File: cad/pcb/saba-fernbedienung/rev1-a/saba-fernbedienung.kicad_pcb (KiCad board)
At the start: 4 copper layers, 100 x 81.8 mm, 230 parts, among them J201 Conn_ARM_JTAG_SWD_10, J301 Conn_01x04, J302 Conn_01x04, J303 Micro_SD_Card, J304 Conn_01x04, J305 AudioJack3, J306 Conn_01x02, J307 Conn_01x04, J308 Conn_01x01, J309 Conn_01x01, J310 Conn_01x01, J311 Conn_01x04, J312 Conn_01x08, J313 USB_C_Receptacle_USB2.0, K601 G6K-2, K602 G6K-2, K603 G6K-2, K604 G6K-2, K605 G6K-2, K606 G6K-2, K607 EC2-5TNU, Q201 BC856, Q601 BC846, Q602 BC846, Q603 BC846, Q604 BC846, Q605 BC846, Q606 BC846, Q607 BC846, U201 DOIT-DEVKITV1-ESP32-WROOM-32, U301 TSOP31238, U401 TEC2-0911, U402 1117 1.8V, U403 1117 3.3V, U501 ADA4522-2, U502 LM339, U503 LTV-357T, U504 LTV-357T, U505 LTV-357T, U601 LTV-357T, U701 AD8656, U702 VS1053, Y701 12,288MHz

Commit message: Sicherung
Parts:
- added REF**: OSHW-Logo2_7.3x6mm_SilkScreen, Symbol:OSHW-Logo2_7.3x6mm_SilkScreen, F.Cu at (106.9, 136.8)
- added REF**: OSHW-Logo2_7.3x6mm_Copper, Symbol:OSHW-Logo2_7.3x6mm_Copper, F.Cu at (106.9, 136.8)
- added REF**: MountingHole_3.2mm_M3, MountingHole:MountingHole_3.2mm_M3, F.Cu at (180.0, 101.5)
- added REF**: MountingHole_3.2mm_M3, MountingHole:MountingHole_3.2mm_M3, F.Cu at (170.0, 101.5)
- added REF**: MountingHole_3.2mm_M3, MountingHole:MountingHole_3.2mm_M3, F.Cu at (109.0, 72.5)
- added REF**: MountingHole_3.2mm_M3, MountingHole:MountingHole_3.2mm_M3, F.Cu at (191.0, 72.5)
- added REF**: MountingHole_3.2mm_M3, MountingHole:MountingHole_3.2mm_M3, F.Cu at (191.0, 130.5)
- added REF**: MountingHole_3.2mm_M3, MountingHole:MountingHole_3.2mm_M3, F.Cu at (109.0, 130.5)
- R205, R206, R207, R208: moved to B.Cu
- moved J312 252.9 mm to (111.2, 119.0), turned to 270 degrees
- moved R504 243.7 mm to (84.9, 175.9)
- moved R520 243.7 mm to (101.4, 165.3)
- moved R524 243.7 mm to (96.9, 172.8)
- moved D502 243.7 mm to (80.6, 172.1)
- moved D505 243.7 mm to (81.1, 165.1)
- moved D506 243.7 mm to (89.2, 160.5)
- moved R512 243.7 mm to (88.9, 163.3)
- moved R514 243.7 mm to (88.9, 178.4)
- moved R515 243.7 mm to (96.8, 170.3)
- moved R523 243.7 mm to (88.9, 180.9)
- moved R525 243.7 mm to (100.8, 170.3)
- moved R526 243.7 mm to (92.9, 178.4)
- moved R527 243.7 mm to (96.9, 175.3)
- moved R531 243.7 mm to (76.9, 178.9)
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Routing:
- net SABA_GND_AC: track 16.0 -> 92.8 mm, vias 0 -> 6
- net SABA_Reserve: track 0.00 -> 63.1 mm, vias 0 -> 1
- net SABA_Laut: track 0.00 -> 44.3 mm
- net Net-(J201-Pad6): track 0.00 -> 43.4 mm, vias 0 -> 1
- net SABA_Leise: track 0.00 -> 40.1 mm
- net IR_RX: track 0.00 -> 34.2 mm
- net SABA_15V_AC: track 13.1 -> 46.8 mm, vias 0 -> 2
- net Earth: track 2.30 -> 34.9 mm, vias 1 -> 13
- net LCD_BL: track 0.00 -> 31.2 mm, vias 0 -> 1
- net SABA_Suchlauf_L: track 0.00 -> 29.5 mm
- net SABA_~15V_AC: track 21.8 -> 49.1 mm
- net ~RESET: track 0.00 -> 27.1 mm
- net Net-(J201-Pad4): track 0.00 -> 19.5 mm
- net SABA_Schnelllauf: track 0.00 -> 19.2 mm
- net Net-(J201-Pad8): track 0.00 -> 19.0 mm
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- added copper zone on In2.Cu, net +24V
- added copper zone on B.Cu, net -24V
- added copper zone on In1.Cu, net SABA_GND_AC

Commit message: Sicherung
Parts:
- moved D302 196.4 mm to (144.2, 77.9), turned to 270 degrees
- moved R308 189.9 mm to (137.1, 69.0), turned to 180 degrees
- moved C302 188.8 mm to (128.4, 80.2)
- moved R306 185.2 mm to (140.0, 70.1), turned to 90 degrees
- moved C301 183.6 mm to (128.5, 77.6)
- moved D303 183.0 mm to (140.8, 77.5), turned to 90 degrees
- moved R303 179.7 mm to (149.8, 55.5)
- moved R307 179.7 mm to (141.7, 70.1), turned to 270 degrees
- moved R304 178.2 mm to (135.9, 74.0), turned to 270 degrees
- moved D301 174.5 mm to (149.3, 46.1)
- moved J308 172.7 mm to (152.6, 41.7)
- moved R302 167.3 mm to (149.9, 52.6)
- moved C303 167.0 mm to (144.7, 69.4)
- moved U601 153.7 mm to (139.9, 108.5), turned to 180 degrees
- moved R301 148.9 mm to (149.0, 49.8)
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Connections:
- R205 pad 2: SABA_Suchlauf_L -> SABA_Schnelllauf
- R207 pad 2: SABA_Schnelllauf -> SABA_Suchlauf_L
- U201 pad 17: SABA_Suchlauf_Schnell -> SABA_HS
- U201 pad 19: SABA_HS -> SABA_Suchlauf_Schnell
- U201 pad 26: SABA_Schnelllauf -> SABA_Suchlauf_L
- U201 pad 27: SABA_Suchlauf_L -> SABA_Schnelllauf
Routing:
- net Net-(C503-Pad1): track 0.00 -> 61.3 mm, vias 0 -> 2
- net Net-(R501-Pad1): track 0.00 -> 60.1 mm, vias 0 -> 2
- net SABA_HS: track 0.00 -> 32.3 mm
- net Net-(C402-Pad2): track 0.00 -> 32.0 mm, vias 0 -> 4
- net +24V: track 14.9 -> 44.8 mm, vias 3 -> 7
- net SABA_GND_AC: track 92.8 -> 120.0 mm, vias 6 -> 11
- net Net-(D503-Pad1): track 2.35 -> 29.2 mm
- net SABA_HS3: track 0.00 -> 25.0 mm, vias 0 -> 1
- net Earth: track 34.9 -> 59.7 mm, vias 13 -> 14
- net Net-(D504-Pad1): track 3.26 -> 25.3 mm, vias 0 -> 2
- net /Suchlauf Messung/Phase: track 0.00 -> 18.9 mm, vias 0 -> 2
- net Net-(R515-Pad2): track 0.00 -> 16.8 mm
- net /Suchlauf Messung/Amplitude: track 4.52 -> 20.3 mm, vias 0 -> 2
- net SABA_6,3V_AC: track 0.00 -> 13.7 mm
- net Net-(C402-Pad1): track 0.00 -> 12.8 mm
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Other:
- outline, holes or cut-outs redrawn
- board text added: "Saba 6-3D Serie Automatik Fernbedienung - Webradio"

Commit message: Sicherung
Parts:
- removed R201, R202: 10k, Resistor_SMD:R_0603_1608Metric
- moved C715 175.6 mm to (47.6, 103.4), turned to 270 degrees
- moved R707 170.5 mm to (53.0, 104.8), turned to 270 degrees
- moved C708 167.6 mm to (54.5, 102.9), turned to 90 degrees
- moved C709 165.9 mm to (54.5, 106.7), turned to 90 degrees
- moved C702 163.8 mm to (62.4, 98.3), turned to 270 degrees
- moved C714 163.3 mm to (47.6, 106.4), turned to 90 degrees
- moved R719 158.7 mm to (63.0, 112.0), turned to 90 degrees
- moved C701 158.5 mm to (59.2, 98.3), turned to 270 degrees
- moved R721 158.4 mm to (56.0, 111.8), turned to 90 degrees
- moved C720 156.5 mm to (66.6, 105.6), turned to 270 degrees
- moved R715 152.9 mm to (77.7, 107.7), turned to 90 degrees
- moved C707 152.6 mm to (60.7, 98.6), turned to 270 degrees
- moved R717 151.3 mm to (75.4, 108.4)
- moved C711 149.8 mm to (69.2, 105.5), turned to 180 degrees
- moved R720 148.9 mm to (55.6, 98.9)
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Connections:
- J311 pad 1: SABA_Reserve -> (no net)
- U201 pad 12: Net-(R201-Pad1) -> (no net)
- U201 pad 15: SABA_Laut -> LCD_A0
- U201 pad 4: LCD_A0 -> SABA_Laut
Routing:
- net Earth: track 59.7 -> 147.9 mm, vias 14 -> 69
- net SABA_Reserve: track 66.7 -> 0.00 mm, vias 1 -> 0
- net LCD_A0: track 0.00 -> 41.6 mm
- net +3.3VA: track 0.00 -> 34.9 mm, vias 0 -> 3
- net +5VA: track 0.00 -> 34.4 mm, vias 0 -> 3
- net SABA_Laut: track 44.3 -> 15.8 mm
- net Net-(C705-Pad2): track 0.00 -> 26.8 mm
- net +3V3: track 5.72 -> 30.7 mm, vias 0 -> 6
- net LCD_BL: track 31.2 -> 6.49 mm, vias 1 -> 0
- net Net-(J313-PadS1): track 0.00 -> 20.7 mm
- net Net-(C303-Pad1): track 0.00 -> 20.2 mm
- net Net-(D301-Pad1): track 0.00 -> 19.0 mm
- net +1V8: track 0.00 -> 18.5 mm, vias 0 -> 2
- net Net-(R705-Pad2): track 0.00 -> 18.0 mm
- net Net-(C716-Pad2): track 0.00 -> 16.9 mm
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- added copper zone on F.Cu, net +5V
- added copper zone on F.Cu, net Earth
- added copper zone on In1.Cu, net Earth
- added copper zone on F.Cu, net Net-(C401-Pad1)
- added copper zone on F.Cu, net Net-(C402-Pad1)
- added copper zone on F.Cu, net Net-(C402-Pad2)
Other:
- outline, holes or cut-outs redrawn

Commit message: Sicherung
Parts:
- moved R719 63.9 mm to (126.6, 105.6), turned to 180 degrees
- moved C414 63.5 mm to (123.6, 107.5)
- moved C717 59.7 mm to (135.1, 94.7)
- moved C721 59.7 mm to (131.9, 102.3)
- moved C722 59.7 mm to (131.9, 103.8)
- moved R716 59.7 mm to (134.9, 102.3)
- moved R717 59.7 mm to (134.9, 103.8)
- moved R718 59.7 mm to (134.9, 98.3)
- moved C703 59.7 mm to (114.0, 105.1)
- moved C704 59.7 mm to (120.4, 107.4)
- moved C707 59.7 mm to (120.2, 94.0)
- moved C708 59.7 mm to (114.0, 98.3)
- moved C709 59.7 mm to (114.0, 102.1)
- moved R707 59.7 mm to (112.5, 100.2)
- moved C417 59.7 mm to (129.6, 97.7)
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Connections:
- J312 pad 4: LCD_A0 -> ~RESET
- J312 pad 8: ~RESET -> LCD_A0
- R206 pad 2: SPI_CS_LCD -> SABA_Leise
- U201 pad 23: SABA_Leise -> SPI_CS_LCD
- U201 pad 3: SPI_CS_LCD -> SABA_Leise
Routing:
- net SPI_MOSI: track 2.86 -> 67.3 mm, vias 1 -> 3
- net SABA_Mute: track 0.00 -> 45.0 mm, vias 0 -> 2
- net Net-(R203-Pad2): track 0.00 -> 38.5 mm, vias 0 -> 1
- net SPI_SCK: track 2.84 -> 39.9 mm
- net ~RESET: track 29.3 -> 65.4 mm
- net SPI_CS_SDCARD: track 0.00 -> 30.8 mm, vias 0 -> 1
- net SPI_CS_VS1053: track 0.00 -> 26.4 mm, vias 0 -> 1
- net SPI_MISO: track 2.24 -> 25.8 mm
- net VS1053_DREQ: track 2.62 -> 14.4 mm
- net SPI_CS_LCD: track 2.10 -> 10.2 mm
- net LCD_A0: track 41.6 -> 34.2 mm
- net Net-(C715-Pad1): track 9.02 -> 12.5 mm
- net LCD_BL: track 6.49 -> 9.88 mm, vias 0 -> 1
- net +1V8: track 18.5 -> 21.8 mm, vias 2 -> 3
- net Net-(C714-Pad1): track 9.21 -> 11.8 mm
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
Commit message: PCB: Alle Leitungen verlegt
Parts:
- C407: footprint Capacitor_THT:CP_Radial_D10.0mm_P5.00mm -> local:CP_Radial_D10.0mm_P5.00mm_liegend
- moved R715 12.3 mm to (127.4, 95.6)
- moved C719 12.0 mm to (127.4, 92.5)
- moved C717 9.91 mm to (125.4, 92.5), turned to 270 degrees
- moved R711 6.70 mm to (125.4, 95.6)
- moved R402 1.95 mm to (109.4, 91.5)
- moved C417 0.43 mm to (129.6, 97.3)
- moved R702 0.36 mm to (116.8, 81.8)
- moved C710 0.17 mm to (116.8, 86.6)
- moved R703 0.17 mm to (116.8, 83.6)
- moved R704 0.17 mm to (116.8, 85.1)
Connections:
- C301 pad 2: Earth -> GND
- C302 pad 2: Earth -> GND
- C303 pad 2: Earth -> GND
- C304 pad 2: Earth -> GND
- C406 pad 2: Earth -> GND
- C407 pad 2: Earth -> GND
- C409 pad 1: Earth -> GND
- C412 pad 2: Earth -> GND
- C413 pad 2: Earth -> GND
- C414 pad 2: Earth -> GND
- C415 pad 2: Earth -> GND
- C416 pad 2: Earth -> GND
- C417 pad 2: Earth -> GND
- C506 pad 1: Earth -> GND
- C507 pad 1: Earth -> GND
- C508 pad 1: Earth -> GND
- C601 pad 1: Earth -> GND
- C701 pad 1: Earth -> GND
- C702 pad 1: Earth -> GND
- C703 pad 1: Earth -> GND
- C704 pad 1: Earth -> GND
- C706 pad 1: Earth -> GND
- C707 pad 1: Earth -> GND
- C708 pad 1: Earth -> GND
- C709 pad 1: Earth -> GND
- C710 pad 1: Earth -> GND
- C711 pad 1: Earth -> GND
- C712 pad 1: Earth -> GND
- C713 pad 1: Earth -> GND
- C714 pad 2: Earth -> GND
- C715 pad 2: Earth -> GND
- C718 pad 2: Earth -> GND
- C720 pad 2: Earth -> GND
- C721 pad 2: Earth -> GND
- C722 pad 2: Earth -> GND
- C723 pad 2: Earth -> GND
- C724 pad 2: Earth -> GND
- C725 pad 2: Earth -> GND
- D201 pad 1: Earth -> GND
- D301 pad 3: Earth -> GND
- D303 pad 2: Earth -> GND
- J201 pad 3: Earth -> GND
- J201 pad 5: Earth -> GND
- J201 pad 9: Earth -> GND
- J303 pad 6: Earth -> GND
- J305 pad T: Earth -> GND
- J308 pad 1: Earth -> GND
- J312 pad 7: Earth -> GND
- J313 pad A1: Earth -> GND
- J313 pad A12: Earth -> GND
- J313 pad B1: Earth -> GND
- J313 pad B12: Earth -> GND
- Q601 pad 2: Earth -> GND
- Q602 pad 2: Earth -> GND
- Q603 pad 2: Earth -> GND
- Q604 pad 2: Earth -> GND
- Q605 pad 2: Earth -> GND
- Q606 pad 2: Earth -> GND
- Q607 pad 2: Earth -> GND
- R304 pad 1: Earth -> GND
- R306 pad 1: Earth -> GND
- R307 pad 2: Earth -> GND
- R308 pad 1: Earth -> GND
- R401 pad 1: Earth -> GND
- R402 pad 1: Earth -> GND
- R604 pad 1: Earth -> GND
- R605 pad 1: Earth -> GND
- R610 pad 1: Earth -> GND
- R611 pad 1: Earth -> GND
- R615 pad 1: Earth -> GND
- R616 pad 1: Earth -> GND
- R623 pad 1: Earth -> GND
- R704 pad 2: Earth -> GND
- R705 pad 1: Earth -> GND
- R706 pad 1: Earth -> GND
- R712 pad 2: Earth -> GND
- R713 pad 1: Earth -> GND
- R714 pad 1: Earth -> GND
- R719 pad 1: Earth -> GND
- R720 pad 1: Earth -> GND
- R721 pad 1: Earth -> GND
- U201 pad 2: Earth -> GND
- U201 pad 29: Earth -> GND
- U301 pad 1: Earth -> GND
- U401 pad 7: Earth -> GND
- U402 pad 1: Earth -> GND
- U403 pad 1: Earth -> GND
- U503 pad 3: Earth -> GND
- U504 pad 3: Earth -> GND
- U505 pad 3: Earth -> GND
- U601 pad 3: Earth -> GND
- U701 pad 4: Earth -> GND
- U702 pad 16: Earth -> GND
- U702 pad 20: Earth -> GND
- U702 pad 21: Earth -> GND
- U702 pad 22: Earth -> GND
- U702 pad 35: Earth -> GND
- U702 pad 37: Earth -> GND
- U702 pad 4: Earth -> GND
- U702 pad 40: Earth -> GND
- U702 pad 41: Earth -> GND
- U702 pad 47: Earth -> GND
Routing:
- net GND: track 0.00 -> 171.5 mm, vias 0 -> 76
- net Earth: track 150.4 -> 17.9 mm, vias 69 -> 0
- net +5V: track 24.7 -> 131.5 mm, vias 2 -> 13
- net SPI_SCK: track 39.9 -> 68.2 mm, vias 1 -> 3
- net SPI_MISO: track 25.8 -> 53.9 mm, vias 1 -> 2
- net SABA_Leise: track 39.8 -> 16.0 mm
- net SPI_DCS_VS1053: track 0.00 -> 21.3 mm, vias 0 -> 2
- net +3V3: track 30.7 -> 48.9 mm, vias 6 -> 12
- net Net-(R715-Pad1): track 12.8 -> 28.6 mm
- net +1V8: track 21.8 -> 35.1 mm, vias 3 -> 6
- net /Audio/links: track 2.26 -> 11.4 mm
- net Net-(R713-Pad2): track 8.14 -> 14.0 mm
- net /Audio/rechts: track 7.87 -> 13.7 mm
- net Net-(R619-Pad2): track 0.00 -> 4.89 mm
- net SABA_Mute: track 45.0 -> 40.7 mm, vias 2 -> 1
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- added copper zone on In2.Cu, net +1V8
- added copper zone on In2.Cu, net +3.3VA
- added copper zone on In2.Cu, net +3V3
- added copper zone on In2.Cu, net +5V
- added copper zone on F.Cu, net GND
- added copper zone on In1.Cu, net GND
- removed copper zone on F.Cu, net Earth
- removed copper zone on In1.Cu, net Earth

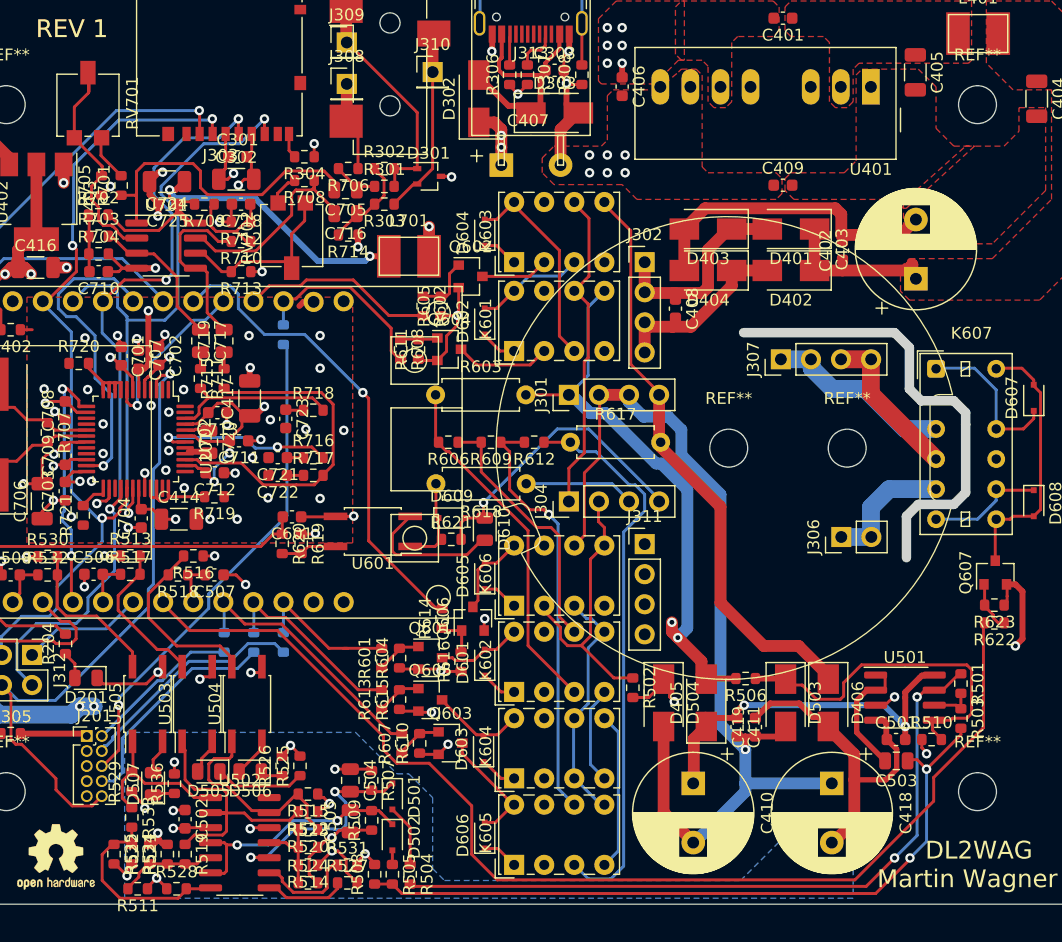
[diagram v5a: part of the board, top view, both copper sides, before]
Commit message: Fix: DRC Fehler
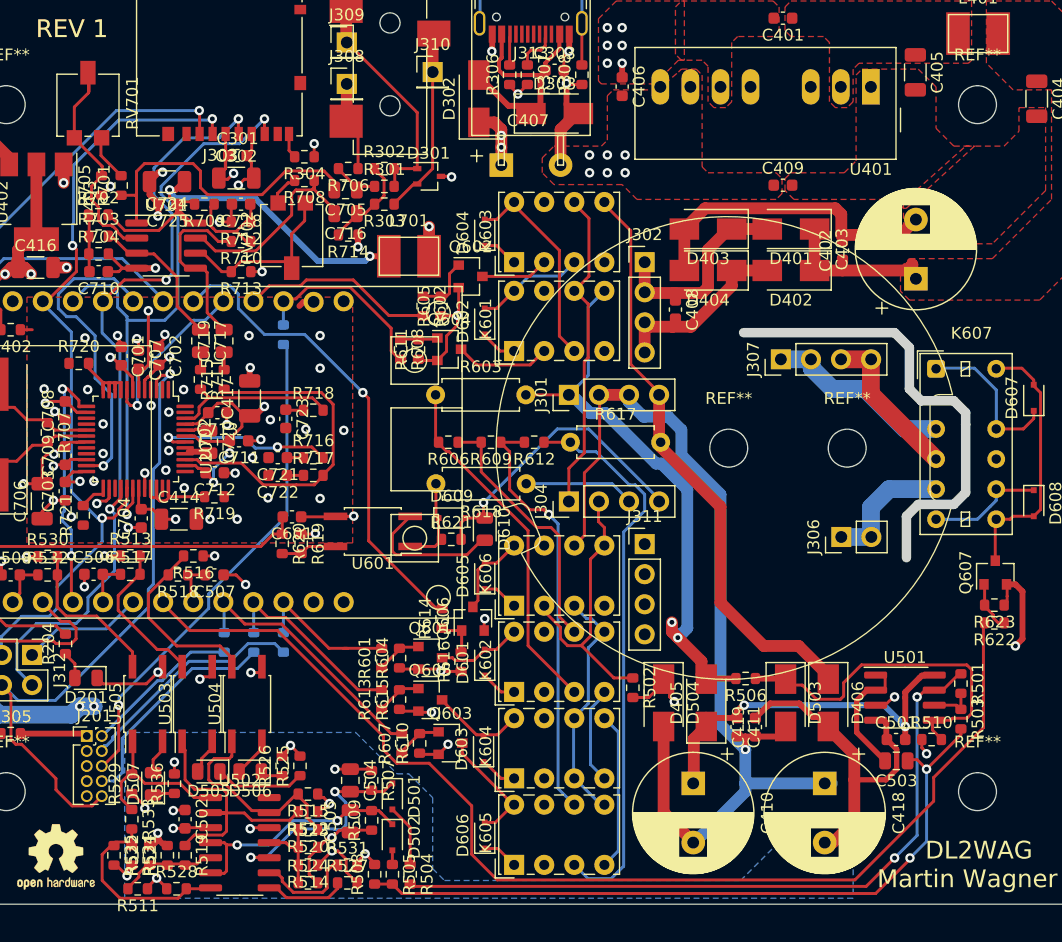
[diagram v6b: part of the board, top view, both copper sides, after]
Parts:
- moved C418 0.60 mm to (178.1, 129.8)
- moved R529 0.15 mm to (119.6, 129.8)
- moved R533 0.15 mm to (119.6, 132.8)
- moved C301 0.10 mm to (128.5, 76.8)
- moved C302 0.10 mm to (128.4, 78.7)
- moved R519 0.10 mm to (124.1, 135.9)
- moved R521 0.10 mm to (122.6, 135.9)
- moved R522 0.10 mm to (121.1, 135.9)
- moved R534 0.10 mm to (119.6, 135.9)
- moved R535 0.10 mm to (118.1, 135.9)
- moved C408 0.08 mm to (165.5, 89.8)
- moved R711 0.08 mm to (125.4, 95.7)
- moved R715 0.08 mm to (127.4, 95.7)
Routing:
- net Net-(R719-Pad2): track 4.87 -> 5.79 mm
- net SABA_GND_AC: track 120.0 -> 120.8 mm
- net Net-(C402-Pad2): track 26.1 -> 26.7 mm

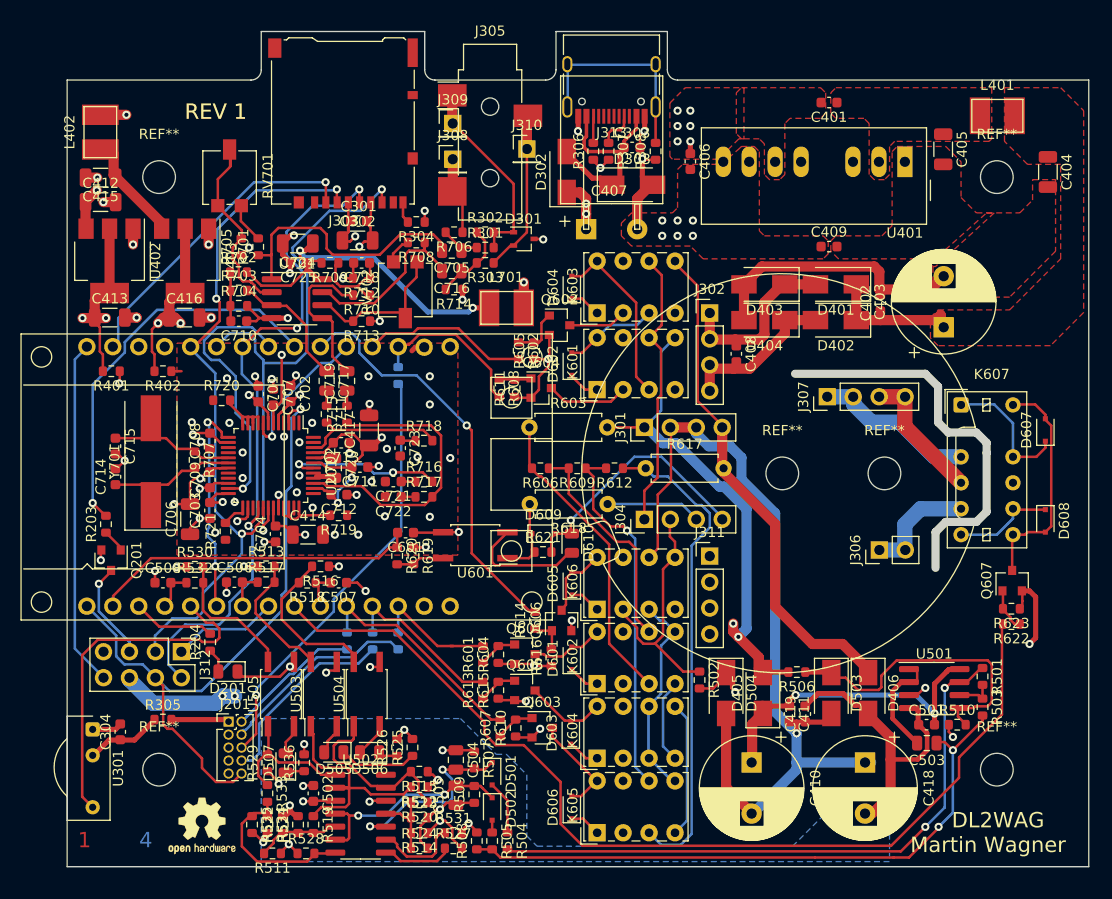
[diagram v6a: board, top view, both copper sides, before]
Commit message: Add: Position Bauteilnummern Druck
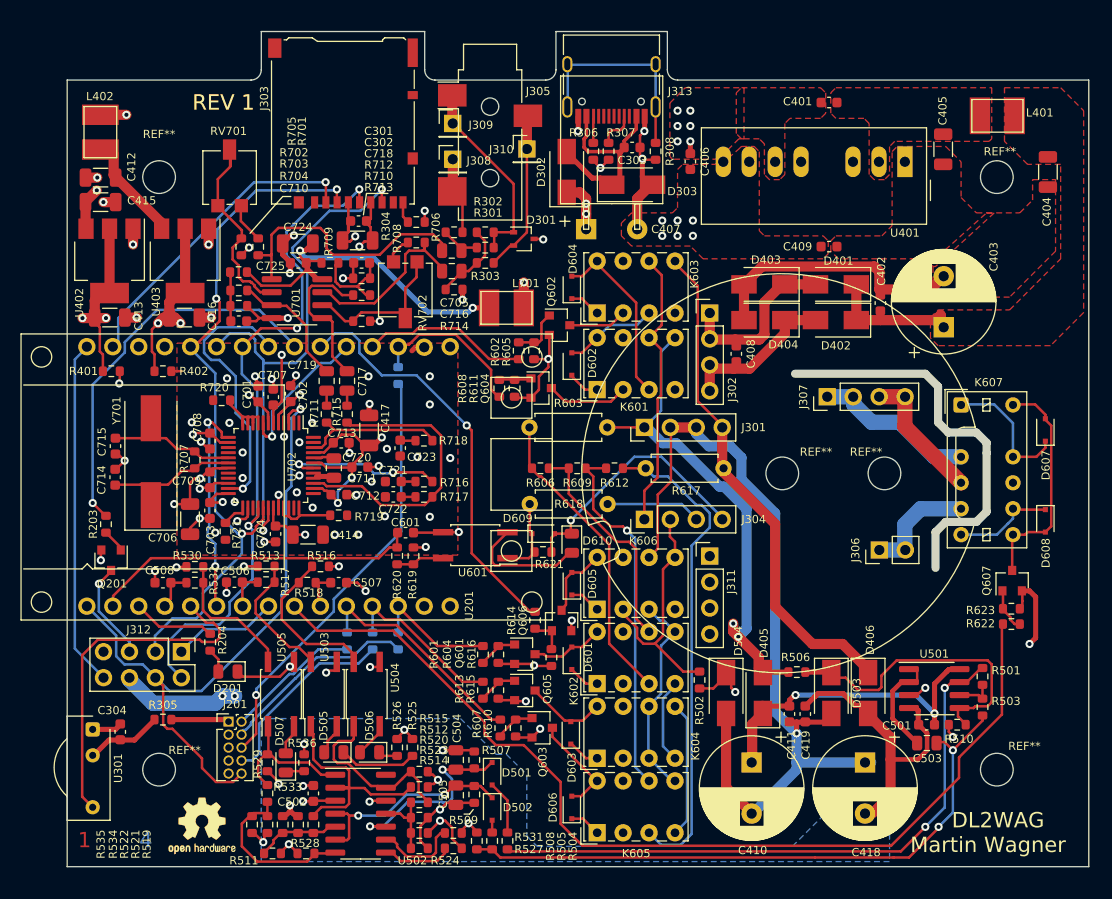
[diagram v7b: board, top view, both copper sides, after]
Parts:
- moved C714 0.05 mm to (104.7, 101.9)
